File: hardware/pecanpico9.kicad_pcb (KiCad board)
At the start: 4 copper layers, 29.8 x 33.7 mm, 111 parts, among them IC1 SPV1040T, IC2 TPS62260DRVR, IC3 ADP322ACPZ-115-R7, IC4 Si4063-B1B-FM, IC5 STM32F413xG, IC6 EVA-7M, IC7 PAC1720-1-AIA-TR, IC8 LDLN015PU33R, IC9 BME280, P1 CONN_01X25, P2 CONN_01X10, P3 ZX62-B-5PA(33), P4 IPX 2mm, P5 CONN_01X02, P6 IPX 2mm, Q1 FDN306P, X1 KT2016K26000BCW18ZAS

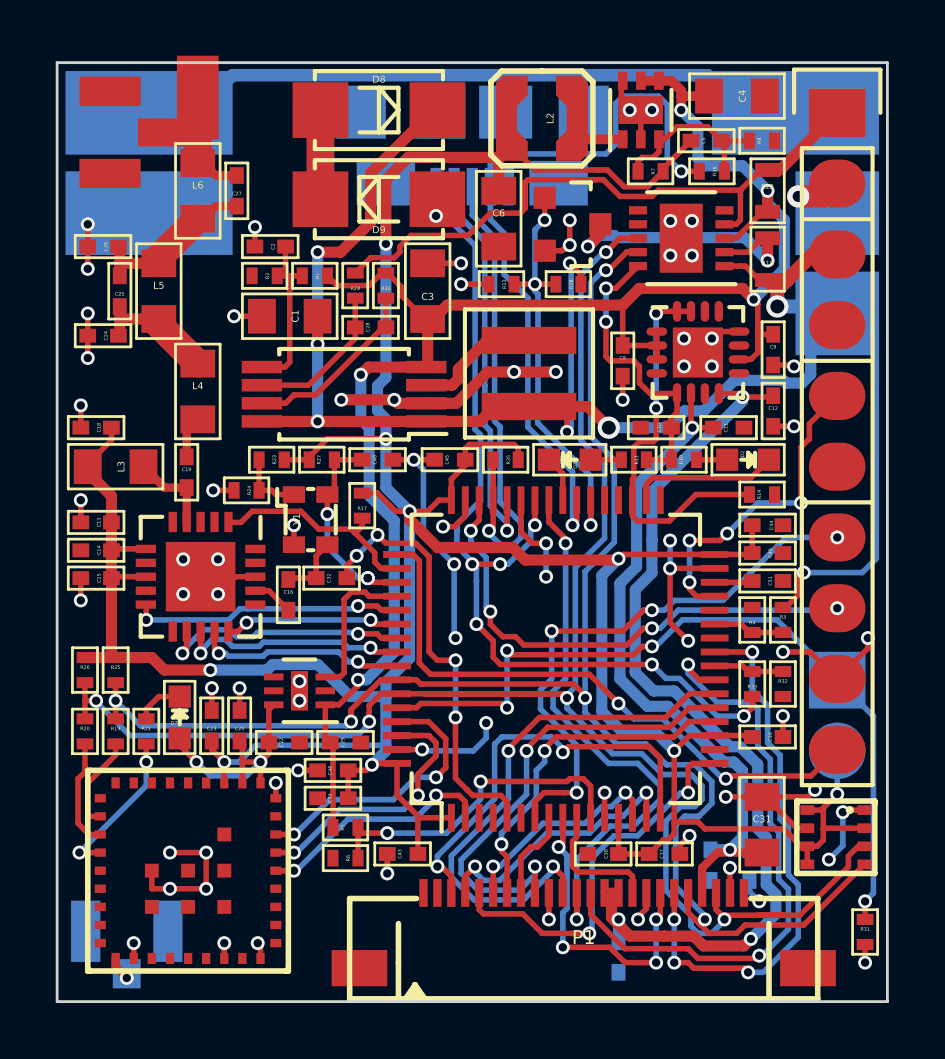
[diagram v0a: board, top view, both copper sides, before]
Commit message: Wiggled traces around, created Gerber
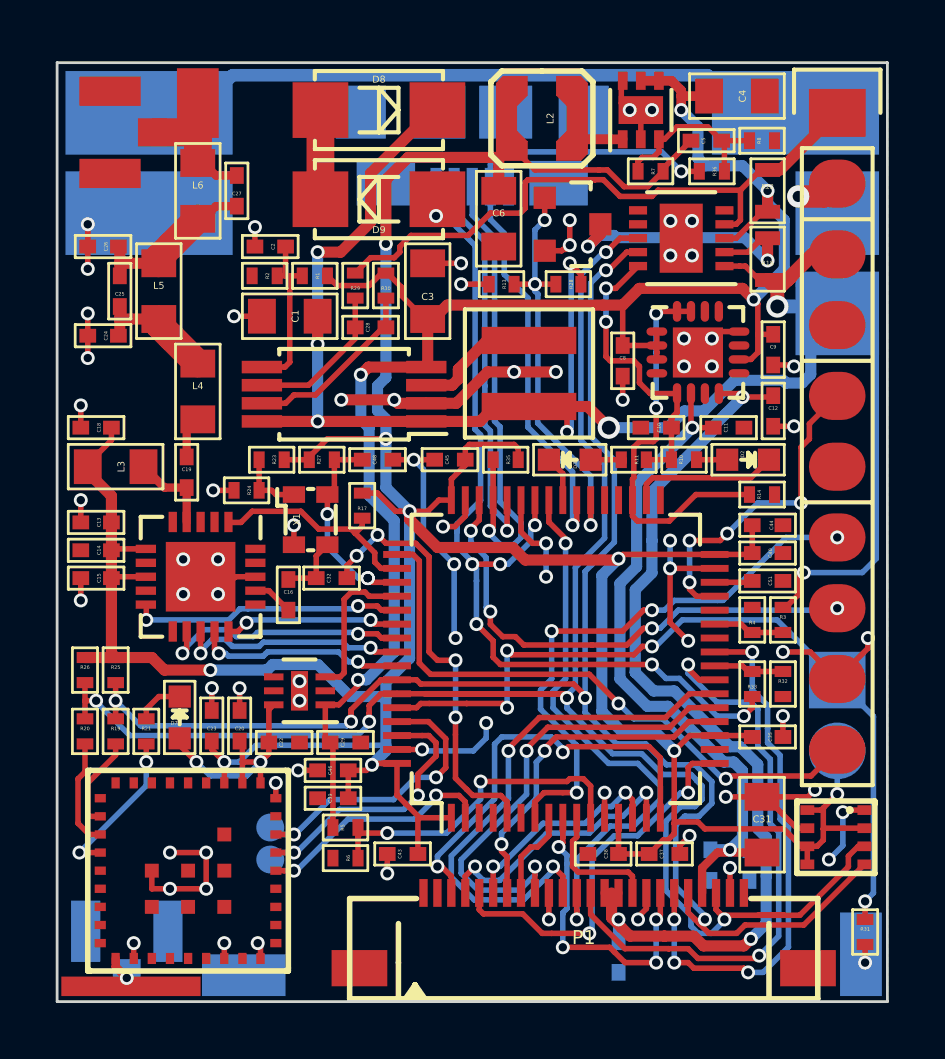
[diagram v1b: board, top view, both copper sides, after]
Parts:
- added W2: Testpad, stm32f7:PAD_3x1.5, B.Cu at (76.0, 122.9)
- added W3: Testpad, stm32f7:PAD_3x1.5, B.Cu at (53.8, 123.7)
- added W4: Testpad, stm32f7:Testpad, B.Cu at (54.8, 118.3)
- added W5: Testpad, stm32f7:Testpad, B.Cu at (54.8, 119.5)
- added W9: Testpad, stm32f7:PAD_3x1.5, F.Cu at (49.8, 124.0)
- moved W1 0.20 mm to (52.1, 92.3)
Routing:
- net /V_BOOST: track 27.4 -> 23.8 mm
- net /GPS_TXD: track 9.61 -> 10.6 mm
- net /GPS_RXD: track 10.2 -> 11.2 mm
- net GND: track 87.9 -> 87.0 mm, vias 75 -> 74
- removed copper zone on In1.Cu, net GND
- removed copper zone on In2.Cu, net GND
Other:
- copper layers 4 -> 2
- net class Default: trace_width 0.2 -> 0.4
- board text added: "GPS UART"

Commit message: Updated BOM
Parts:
- C32: value 10nF -> 10n
- C5: value 22pF -> 22p
- L3: value 470nH -> 470n
- R36, R8: value 250k -> 249k
- R7: value 500k -> 510k
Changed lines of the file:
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@@
     (links 325)
     (no_connects 0)
-    (area 37.303263 85.05 86.538978 125.598275)
+    (area 47.049999 90.849999 76.950001 124.650001)
     (thickness 1)
     (drawings 32)
@@
       (effects (font (size 0.127 0.127) (thickness 0.01875)))
     )
-    (fp_text value 10nF (at 0.1 0 90) (layer F.Fab)
+    (fp_text value 10n (at 0.1 0 90) (layer F.Fab)
       (effects (font (size 0.127 0.127) (thickness 0.015875)))
     )
@@
       (effects (font (size 0.127 0.127) (thickness 0.01875)))
     )
-    (fp_text value 250k (at 0.1 0 90) (layer F.Fab)
+    (fp_text value 249k (at 0.1 0 90) (layer F.Fab)
       (effects (font (size 0.127 0.127) (thickness 0.01875)))
     )
@@
       (effects (font (size 0.127 0.127) (thickness 0.01875)))
     )
-    (fp_text value 22pF (at 0.1 0 90) (layer F.Fab)
+    (fp_text value 22p (at 0.1 0 90) (layer F.Fab)
       (effects (font (size 0.127 0.127) (thickness 0.015875)))
     )
@@
       (effects (font (size 0.127 0.127) (thickness 0.01875)))
     )
-    (fp_text value 500k (at 0.1 0 270) (layer F.Fab)
+    (fp_text value 510k (at 0.1 0 270) (layer F.Fab)
       (effects (font (size 0.127 0.127) (thickness 0.01875)))
     )
@@
       (effects (font (size 0.127 0.127) (thickness 0.01875)))
     )
-    (fp_text value 250k (at 0.1 0 270) (layer F.Fab)
+    (fp_text value 249k (at 0.1 0 270) (layer F.Fab)
       (effects (font (size 0.127 0.127) (thickness 0.01875)))
     )
@@
       (effects (font (size 0.25 0.25) (thickness 0.0375)))
     )
-    (fp_text value 470nH (at 0.2 0 270) (layer F.Fab)
+    (fp_text value 470n (at 0.2 0 270) (layer F.Fab)
       (effects (font (size 0.25 0.25) (thickness 0.0375)))
     )
